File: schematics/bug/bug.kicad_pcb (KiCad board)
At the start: 2 copper layers, 15 parts, among them P1 CONN_01X09, P3 CONN_01X06, P4 CONN_01X02, U1 uln2803A, U2 Arduino_Mini, U3 SPX2920U-3.3, U4 ESP8266, U5 button

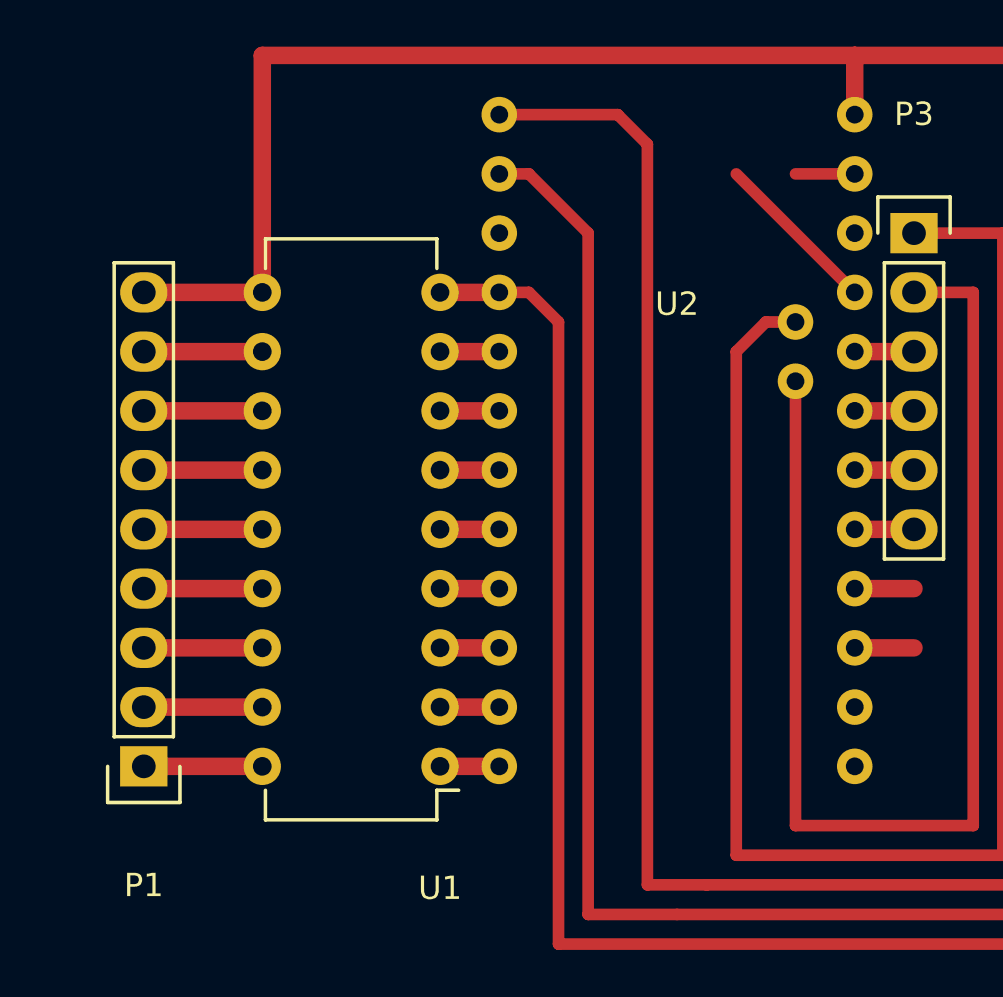
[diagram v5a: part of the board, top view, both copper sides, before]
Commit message: Rewrite lineSensors scheme and small update bug
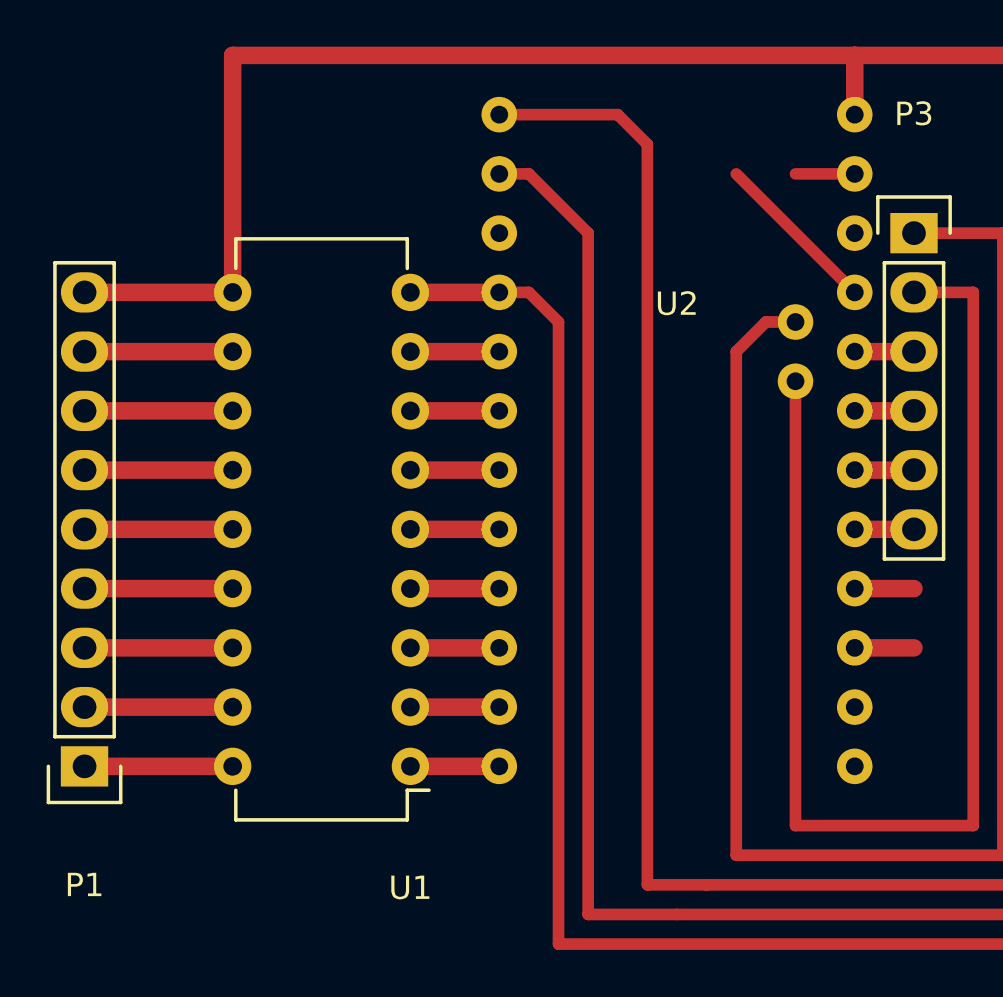
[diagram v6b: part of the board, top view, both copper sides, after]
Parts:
- moved P1 2.54 mm to (114.3, 124.5)
- moved U1 1.27 mm to (128.3, 124.5)
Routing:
- net Net-(P1-Pad9): track 81.3 -> 83.8 mm
- net Net-(P1-Pad8): track 5.08 -> 6.35 mm
- net Net-(P1-Pad7): track 5.08 -> 6.35 mm
- net Net-(P1-Pad6): track 5.08 -> 6.35 mm
- net Net-(P1-Pad5): track 5.08 -> 6.35 mm
- net Net-(P1-Pad4): track 5.08 -> 6.35 mm
- net Net-(P1-Pad3): track 5.08 -> 6.35 mm
- net Net-(P1-Pad2): track 5.08 -> 6.35 mm
- net Net-(P1-Pad1): track 5.08 -> 6.35 mm
- net Net-(U1-Pad8): track 2.54 -> 3.81 mm
- net Net-(U1-Pad7): track 2.54 -> 3.81 mm
- net Net-(U1-Pad6): track 2.54 -> 3.81 mm
- net Net-(U1-Pad5): track 2.54 -> 3.81 mm
- net Net-(U1-Pad4): track 2.54 -> 3.81 mm
- net Net-(U1-Pad3): track 2.54 -> 3.81 mm
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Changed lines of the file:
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@@
     (links 47)
     (no_connects 0)
-    (area 106.579999 37.999999 182.980001 140.150002)
+    (area 106.579999 37.999999 182.980001 137.260001)
     (thickness 1.6)
     (drawings 10)
-    (tracks 103)
+    (tracks 104)
     (zones 0)
     (modules 15)
@@
   )
   (module Housings_DIP:DIP-18_W7.62mm (layer F.Cu)
-    (at 129.54 124.46 180)
+    (at 128.27 124.46 180)
     (descr "18-lead dip package, row spacing 7.62 mm (300 mils)")
     (tags "dil dip 2.54 300")
@@
   )
   (module Pin_Headers:Pin_Header_Straight_1x09 (layer F.Cu)
-    (at 116.84 124.46 180)
+    (at 114.3 124.46 180)
     (descr "Through hole pin header")
     (tags "pin header")
@@
   (segment (start 157.48 109.22) (end 158.75 107.95) (width 0.75) (layer F.Cu) (net 1))
   (segment (start 157.48 114.3) (end 157.48 109.22) (width 0.75) (layer F.Cu) (net 1))
+  (segment (start 132.08 104.14) (end 128.27 104.14) (width 0.75) (layer F.Cu) (net 2) (status C00000))
   (segment (start 134.62 132.08) (end 177.8 132.08) (width 0.5) (layer F.Cu) (net 2))
   (segment (start 167.64 110.49) (end 168.91 111.76) (width 0.5) (layer F.Cu) (net 2))
@@
   (segment (start 175.26 116.84) (end 172.72 116.84) (width 0.5) (layer F.Cu) (net 2))
   (segment (start 175.26 124.46) (end 175.26 116.84) (width 0.5) (layer F.Cu) (net 2))
-  (segment (start 132.08 104.14) (end 129.54 104.14) (width 0.75) (layer F.Cu) (net 2))
   (segment (start 167.64 121.92) (end 172.72 121.92) (width 0.75) (layer F.Cu) (net 3))
   (segment (start 172.72 119.38) (end 170.18 119.38) (width 0.75) (layer F.Cu) (net 4))
-  (segment (start 116.84 124.46) (end 121.92 124.46) (width 0.75) (layer F.Cu) (net 5))
-  (segment (start 116.84 121.92) (end 121.92 121.92) (width 0.75) (layer F.Cu) (net 6))
-  (segment (start 121.92 119.38) (end 116.84 119.38) (width 0.75) (layer F.Cu) (net 7))
-  (segment (start 116.84 116.84) (end 121.92 116.84) (width 0.75) (layer F.Cu) (net 8))
-  (segment (start 121.92 114.3) (end 116.84 114.3) (width 0.75) (layer F.Cu) (net 9))
-  (segment (start 116.84 111.76) (end 121.92 111.76) (width 0.75) (layer F.Cu) (net 10))
-  (segment (start 121.92 109.22) (end 116.84 109.22) (width 0.75) (layer F.Cu) (net 11))
-  (segment (start 116.84 106.68) (end 121.92 106.68) (width 0.75) (layer F.Cu) (net 12))
+  (segment (start 120.65 124.46) (end 114.3 124.46) (width 0.75) (layer F.Cu) (net 5) (status C00000))
+  (segment (start 114.3 121.92) (end 120.65 121.92) (width 0.75) (layer F.Cu) (net 6) (status C00000))
+  (segment (start 120.65 119.38) (end 114.3 119.38) (width 0.75) (layer F.Cu) (net 7) (status C00000))
+  (segment (start 114.3 116.84) (end 120.65 116.84) (width 0.75) (layer F.Cu) (net 8) (status C00000))
+  (segment (start 120.65 116.84) (end 120.65 116.84) (width 0.75) (layer F.Cu) (net 8) (status C00000))
+  (segment (start 120.65 114.3) (end 114.3 114.3) (width 0.75) (layer F.Cu) (net 9) (status C00000))
+  (segment (start 114.3 111.76) (end 120.65 111.76) (width 0.75) (layer F.Cu) (net 10) (status C00000))
+  (segment (start 120.65 109.22) (end 114.3 109.22) (width 0.75) (layer F.Cu) (net 11) (status C00000))
+  (segment (start 114.3 106.68) (end 120.65 106.68) (width 0.75) (layer F.Cu) (net 12) (status C00000))
+  (segment (start 120.65 104.14) (end 114.3 104.14) (width 0.75) (layer F.Cu) (net 13) (status C00000))
+  (segment (start 120.65 93.98) (end 120.65 104.14) (width 0.75) (layer F.Cu) (net 13) (status 800000))
   (segment (start 157.48 93.98) (end 147.32 93.98) (width 0.75) (layer F.Cu) (net 13))
   (segment (start 157.48 99.06) (end 157.48 93.98) (width 0.75) (layer F.Cu) (net 13))
@@
   (segment (start 172.72 101.6) (end 167.64 101.6) (width 0.5) (layer F.Cu) (net 13))
   (segment (start 147.32 96.52) (end 147.32 93.98) (width 0.75) (layer F.Cu) (net 13))
-  (segment (start 121.92 93.98) (end 121.92 104.14) (width 0.75) (layer F.Cu) (net 13))
-  (segment (start 147.32 93.98) (end 121.92 93.98) (width 0.75) (layer F.Cu) (net 13))
-  (segment (start 116.84 104.14) (end 121.92 104.14) (width 0.75) (layer F.Cu) (net 13))
+  (segment (start 147.32 93.98) (end 120.65 93.98) (width 0.75) (layer F.Cu) (net 13))
   (segment (start 142.24 128.27) (end 153.67 128.27) (width 0.5) (layer F.Cu) (net 14))
   (segment (start 144.78 105.41) (end 143.51 105.41) (width 0.5) (layer F.Cu) (net 14))
@@
   (segment (start 162.56 110.49) (end 162.56 114.3) (width 0.75) (layer F.Cu) (net 22))
   (segment (start 162.56 119.38) (end 162.56 116.84) (width 0.75) (layer F.Cu) (net 23))
-  (segment (start 132.08 124.46) (end 129.54 124.46) (width 0.75) (layer F.Cu) (net 24))
-  (segment (start 129.54 121.92) (end 132.08 121.92) (width 0.75) (layer F.Cu) (net 25))
-  (segment (start 132.08 119.38) (end 129.54 119.38) (width 0.75) (layer F.Cu) (net 26))
-  (segment (start 129.54 116.84) (end 132.08 116.84) (width 0.75) (layer F.Cu) (net 27))
-  (segment (start 132.08 114.3) (end 129.54 114.3) (width 0.75) (layer F.Cu) (net 28))
-  (segment (start 129.54 111.76) (end 132.08 111.76) (width 0.75) (layer F.Cu) (net 29))
-  (segment (start 132.08 109.22) (end 129.54 109.22) (width 0.75) (layer F.Cu) (net 30))
-  (segment (start 129.54 106.68) (end 132.08 106.68) (width 0.75) (layer F.Cu) (net 31))
+  (segment (start 132.08 124.46) (end 128.27 124.46) (width 0.75) (layer F.Cu) (net 24))
+  (segment (start 128.27 121.92) (end 132.08 121.92) (width 0.75) (layer F.Cu) (net 25))
+  (segment (start 132.08 119.38) (end 128.27 119.38) (width 0.75) (layer F.Cu) (net 26))
+  (segment (start 128.27 116.84) (end 132.08 116.84) (width 0.75) (layer F.Cu) (net 27))
+  (segment (start 132.08 114.3) (end 128.27 114.3) (width 0.75) (layer F.Cu) (net 28))
+  (segment (start 128.27 111.76) (end 132.08 111.76) (width 0.75) (layer F.Cu) (net 29))
+  (segment (start 132.08 109.22) (end 128.27 109.22) (width 0.75) (layer F.Cu) (net 30))
+  (segment (start 128.27 106.68) (end 132.08 106.68) (width 0.75) (layer F.Cu) (net 31) (status C00000))
   (segment (start 147.32 116.84) (end 149.86 116.84) (width 0.75) (layer F.Cu) (net 33))
   (segment (start 149.86 116.84) (end 149.86 116.84) (width 2) (layer F.Cu) (net 33))

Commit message: Update schematic
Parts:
- removed U5: button, button
- added P2: CONN_01X04, Pin_Headers:Pin_Header_Straight_1x04, F.Cu at (151.1, 116.8)
- added P5: CONN_01X01, Socket_Strips:Socket_Strip_Straight_1x01, F.Cu at (116.8, 96.5)
- added P6: CONN_01X01, Socket_Strips:Socket_Strip_Straight_1x01, F.Cu at (116.8, 99.1)
- added P7: CONN_01X02, Pin_Headers:Pin_Header_Straight_1x02, F.Cu at (170.2, 101.6)
- added R5: R, Resistors_ThroughHole:Resistor_Horizontal_RM7mm, F.Cu at (128.3, 99.1)
- R2, R3: footprint w_pth_resistors:rc05_vert -> w_pth_resistors:RC03
- moved R1 5.08 mm to (165.1, 127.0)
- moved R4 5.08 mm to (165.1, 124.5)
- moved U4 5.08 mm to (162.6, 121.9)
- moved R2 2.54 mm to (160.0, 111.8)
- moved R3 2.54 mm to (162.6, 111.8)
- moved D2 2.54 mm to (172.7, 119.4)
- moved P3 1.27 mm to (151.1, 101.6)
- turned D1 to 270 degrees
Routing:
- net Net-(P5-Pad1): track 7.18 -> 35.2 mm
- net Net-(P1-Pad9): track 83.8 -> 92.7 mm
- net Net-(C1-Pad2): track 152.1 -> 159.6 mm
- net Net-(U2-Pad35): track 70.4 -> 65.3 mm
- net Net-(C1-Pad1): track 19.7 -> 24.8 mm
- net Net-(P6-Pad1): track 0.00 -> 3.81 mm
- net Net-(P2-Pad4): track 0.00 -> 3.81 mm
- net Net-(P2-Pad3): track 0.00 -> 3.81 mm
- net Net-(U2-Pad8): track 2.54 -> 0.00 mm
- net Net-(P4-Pad1): track 7.62 -> 5.08 mm
- net Net-(D2-Pad2): track 2.54 -> 4.71 mm
- net Net-(P3-Pad1): track 66.6 -> 67.8 mm
- net Net-(P3-Pad6): track 2.54 -> 3.81 mm
- net Net-(P3-Pad5): track 2.54 -> 3.81 mm
- net Net-(P3-Pad4): track 2.54 -> 3.81 mm
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
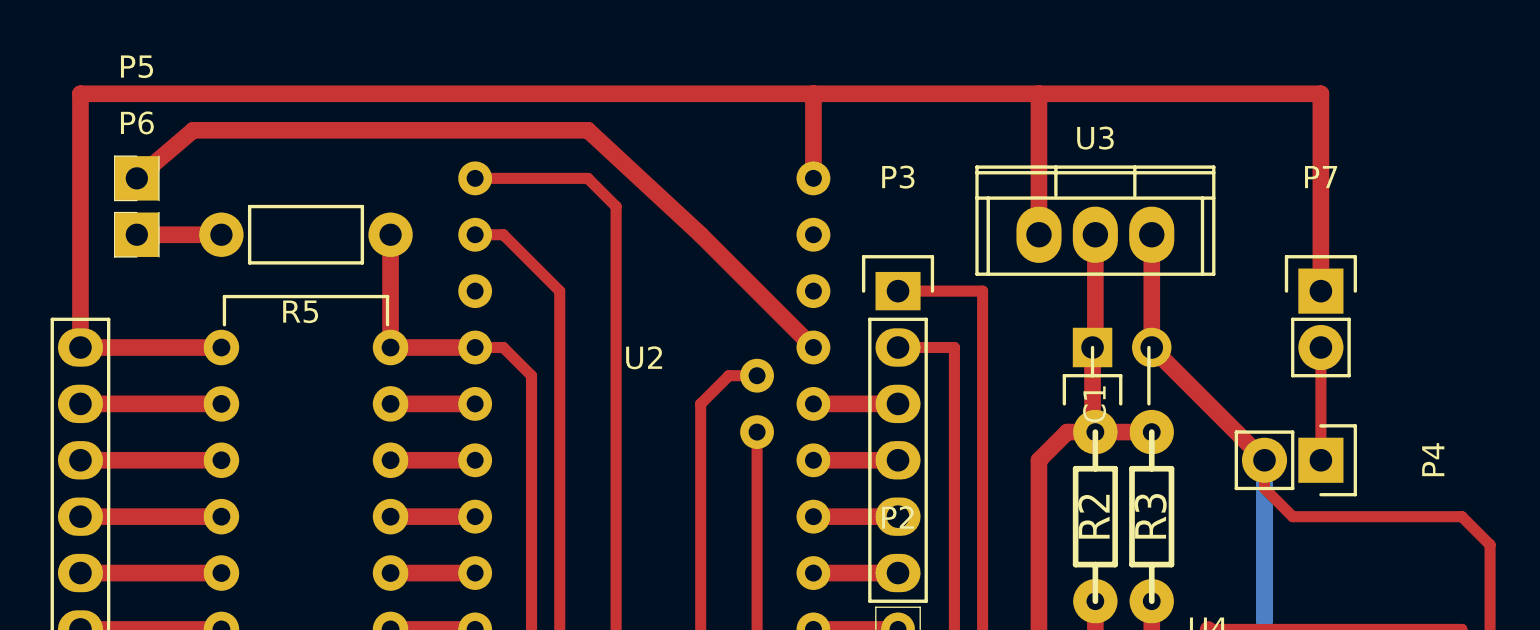
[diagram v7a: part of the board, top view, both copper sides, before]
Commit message: Update schematics for whiskers
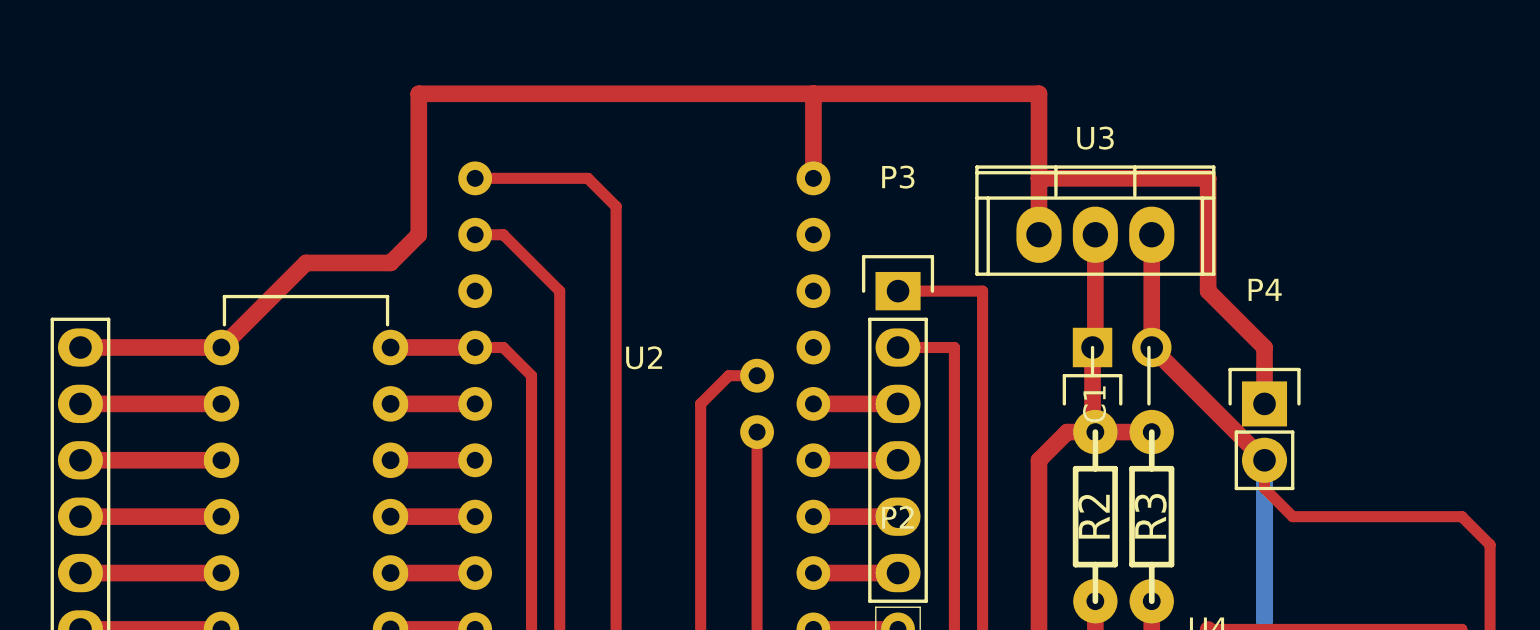
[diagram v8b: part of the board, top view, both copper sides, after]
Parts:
- removed P5, P6: CONN_01X01, Socket_Strips:Socket_Strip_Straight_1x01
- removed P7: CONN_01X02, Pin_Headers:Pin_Header_Straight_1x02
- removed R5: R, Resistors_ThroughHole:Resistor_Horizontal_RM7mm
- moved P4 3.59 mm to (167.6, 106.7), turned to 0 degrees
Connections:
- P4 pad 1: Net-(P4-Pad1) -> Net-(P1-Pad9)
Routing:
- net Net-(U2-Pad10): track 35.2 -> 0.00 mm
- net Net-(P1-Pad9): track 92.7 -> 80.6 mm
- net Net-(P4-Pad1): track 5.08 -> 0.00 mm
- net Net-(C1-Pad2): track 159.6 -> 154.5 mm
- net Net-(P6-Pad1): track 3.81 -> 0.00 mm
